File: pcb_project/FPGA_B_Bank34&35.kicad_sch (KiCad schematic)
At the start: 16 parts, among them U1 XC7A100T-FTG256

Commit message: LED & FPGA_Started
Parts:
- removed C26: 330µF, symbol Device:C
- removed C27, C28, C29, C30, C31, C32: 4.7µF, symbol Device:C
- removed C33, C34, C35, C36, C37, C38, C39, C40: 0.47µF, symbol Device:C
- removed U1: XC7A100T-FTG256, symbol FPGA_Xilinx_Artix7:XC7A100T-FTG256
- added U1: XC7A100T-FTG256, symbol FPGA_Xilinx_Artix7:XC7A100T-FTG256
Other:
- removed sheet A_Bank14&15
- removed sheet B_Bank34&35

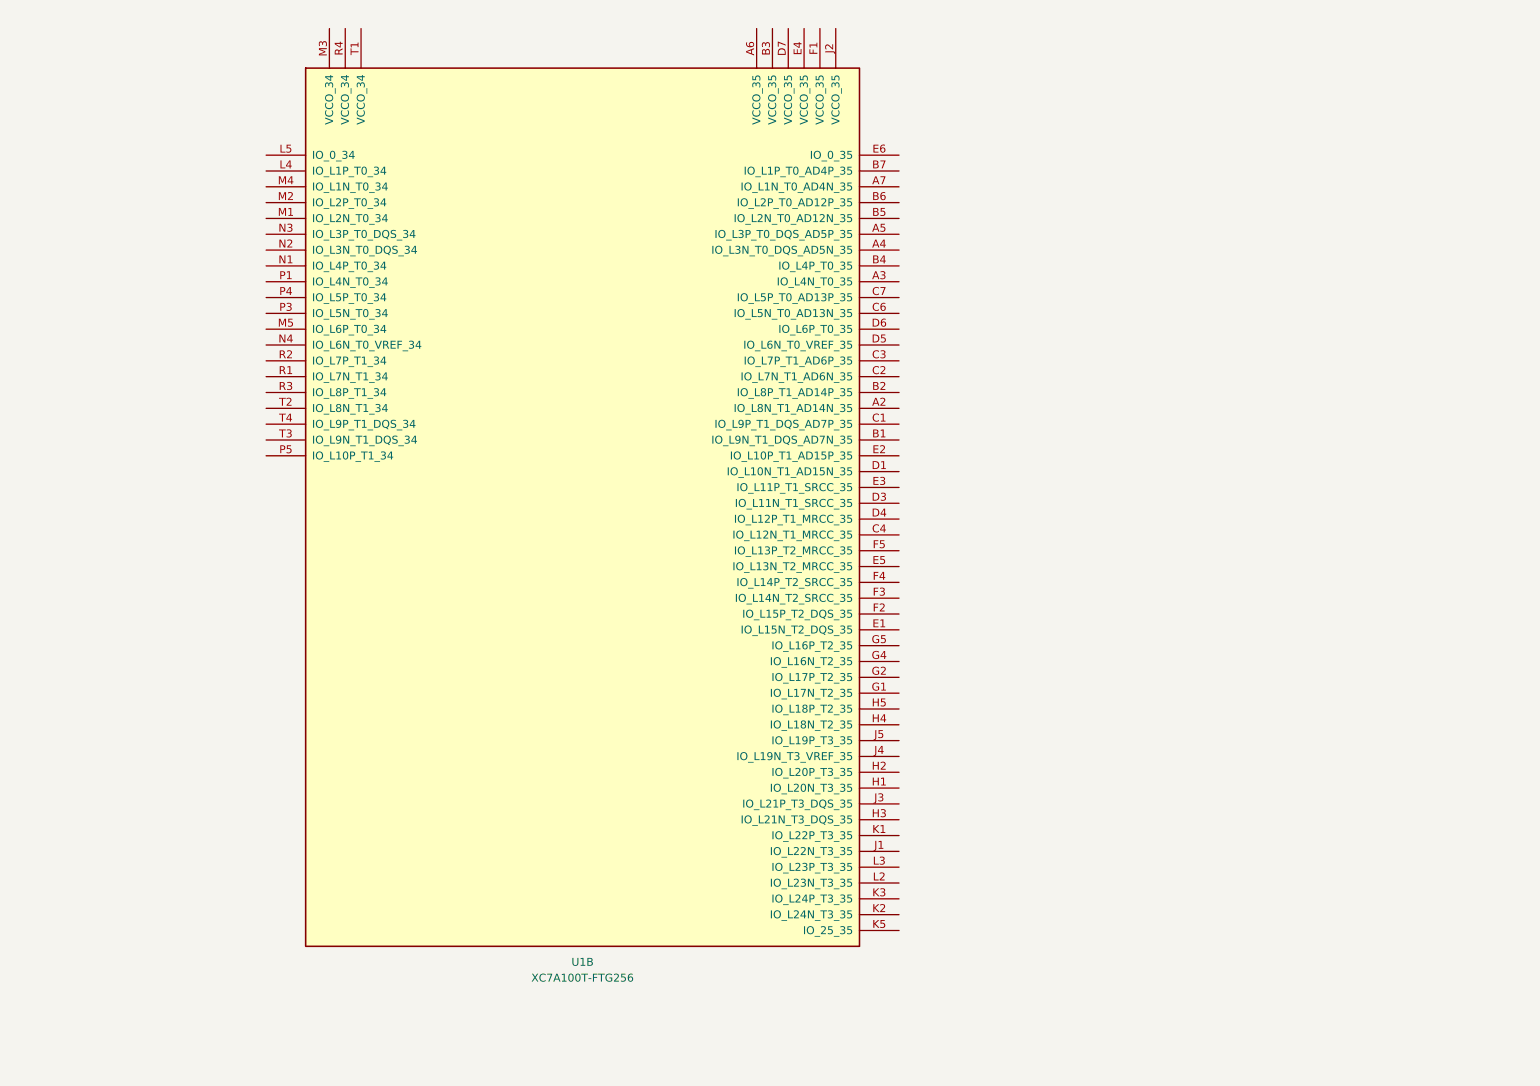
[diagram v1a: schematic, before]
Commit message: Crystal + SPI flash FPGA
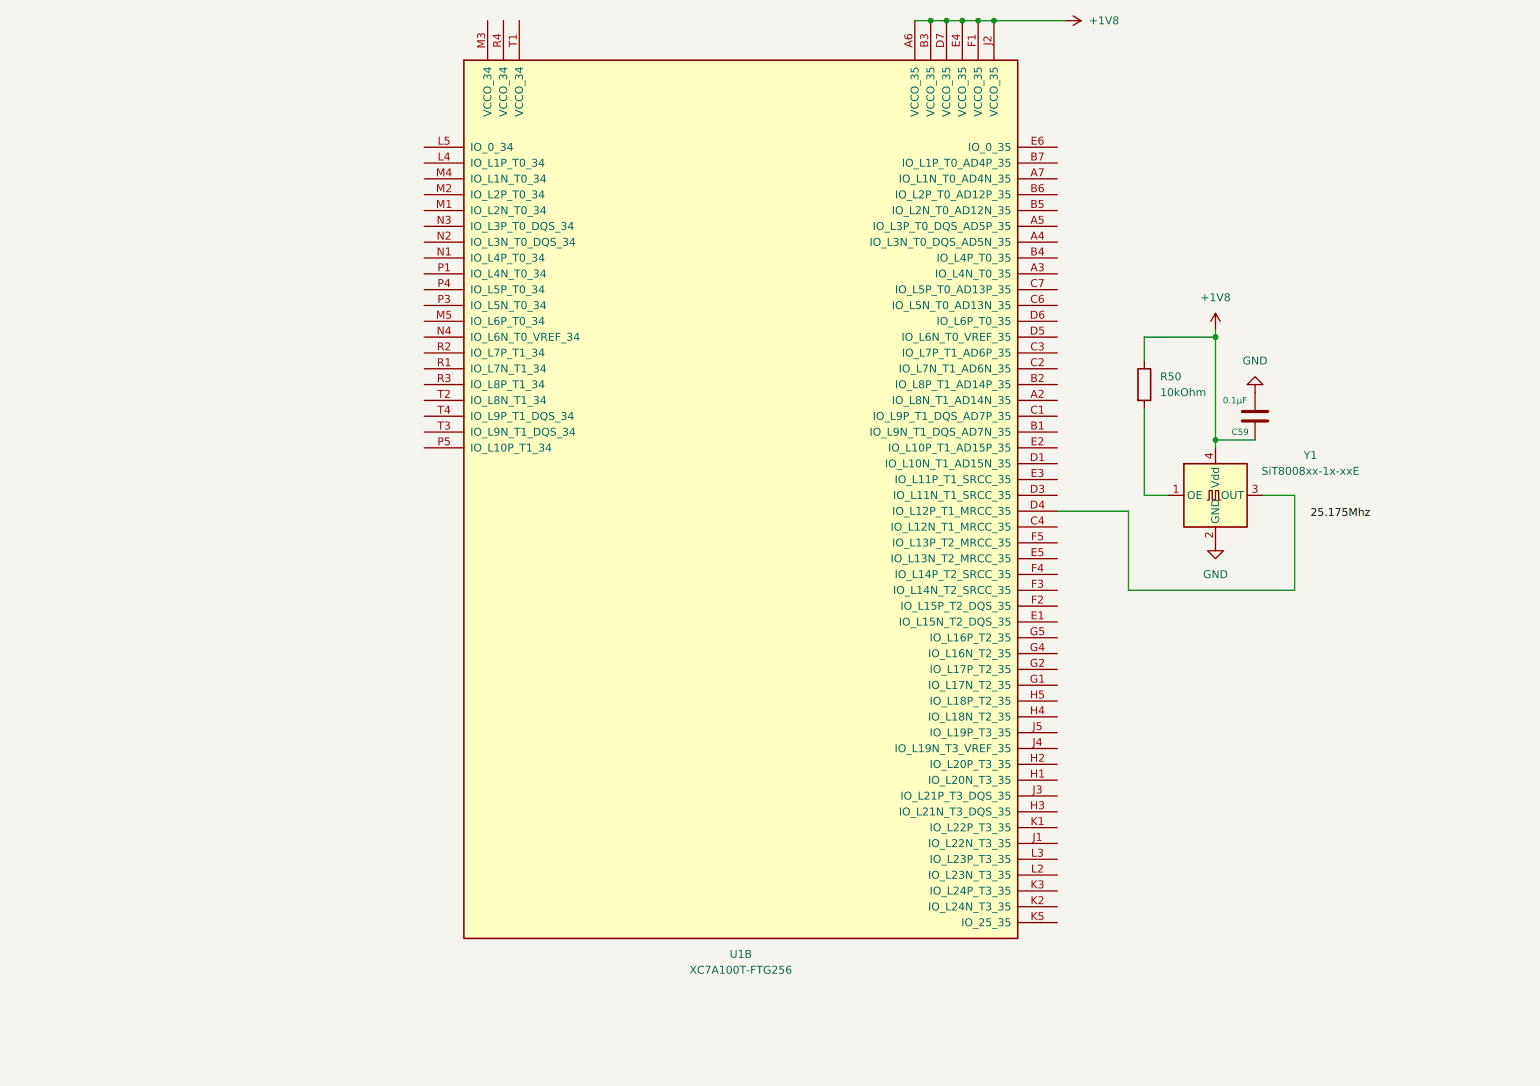
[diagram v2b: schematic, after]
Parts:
- added C59: 0.1µF, symbol Device:C
- added R50: 10kOhm, symbol Device:R
- added Y1: SiT8008xx-1x-xxE, Oscillator:Oscillator_SMD_SiT_PQFN-4Pin_2.5x2.0mm, symbol Oscillator:SiT8008xx-1x-xxE
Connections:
- net +1V8: now reaches U1.A6 (VCCO_35)
- net +1V8: now also U1.B3 (VCCO_35), U1.D7 (VCCO_35), U1.E4 (VCCO_35), U1.F1 (VCCO_35), U1.J2 (VCCO_35), C59.1, R50.1, Y1.4 (Vdd)
- net at U1.D4 (IO_L12P_T1_MRCC_35): now also Y1.3 (OUT)
- new net: R50.2, Y1.1 (OE)
- new net GND: C59.2, Y1.2 (GND)
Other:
- moved on the sheet: U1B

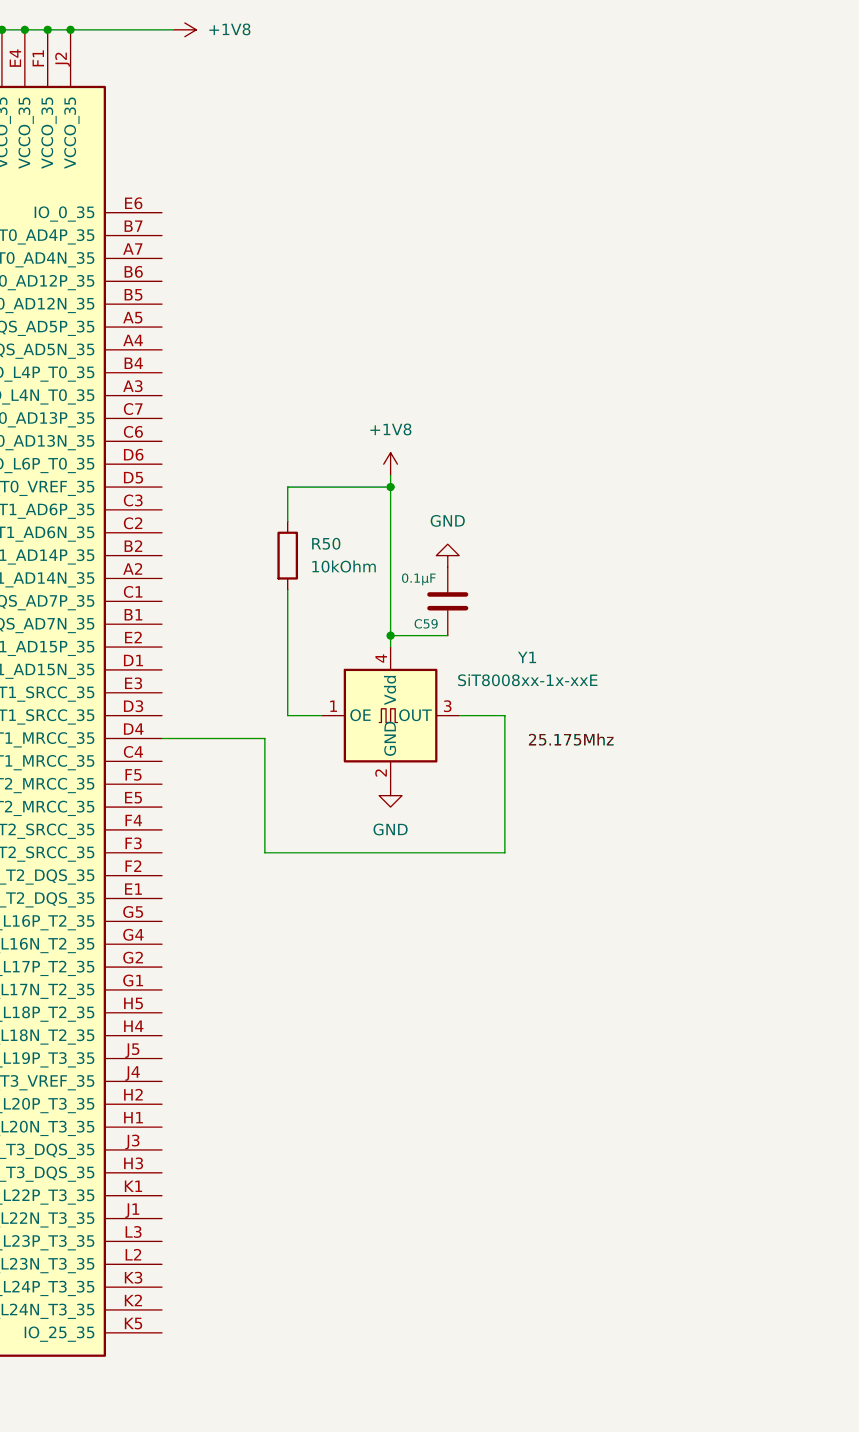
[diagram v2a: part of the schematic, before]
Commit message: VGA Root + Change FPGA Oscilator to 3.3v
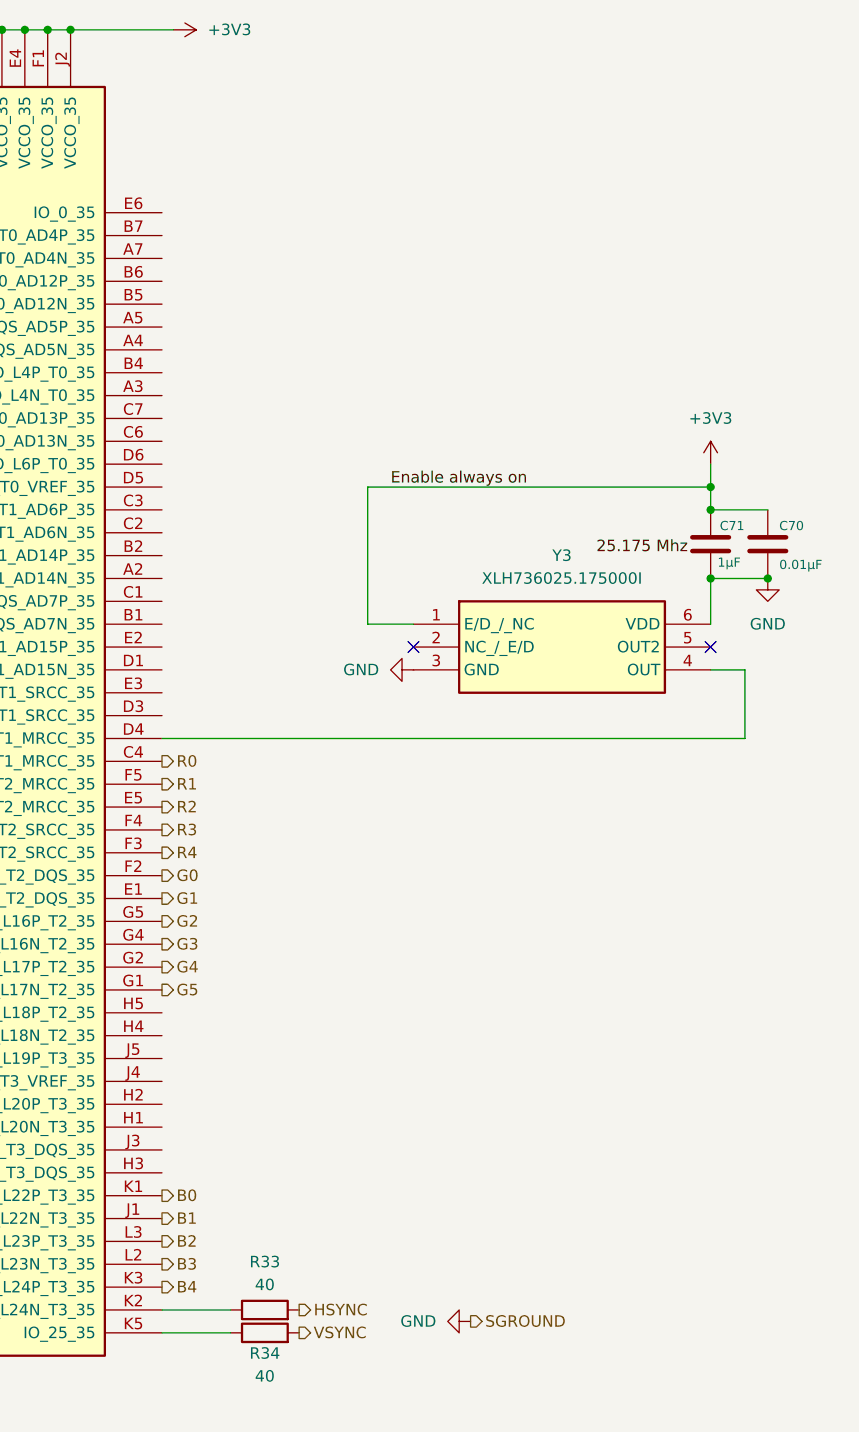
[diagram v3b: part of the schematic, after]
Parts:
- removed C59: 0.1µF, symbol Device:C
- removed R50: 10kOhm, symbol Device:R
- removed Y1: SiT8008xx-1x-xxE, Oscillator:Oscillator_SMD_SiT_PQFN-4Pin_2.5x2.0mm, symbol Oscillator:SiT8008xx-1x-xxE
- added C70: 0.01µF, symbol Device:C
- added C71: 1µF, symbol Device:C
- added R33, R34: 40, symbol Device:R
- added Y3: XLH736025.175000I, XLH730003580000I, symbol XLH736025_175000I:XLH736025.175000I
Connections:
- net GND: now also C70.2, C71.2, Y3.3 (GND), Y3.6 (VDD)
- net at U1.D4 (IO_L12P_T1_MRCC_35): now also Y3.4 (OUT)
- net R0: now reaches U1.C4 (IO_L12N_T1_MRCC_35)
- net G1: now reaches U1.E1 (IO_L15N_T2_DQS_35)
- net R2: now reaches U1.E5 (IO_L13N_T2_MRCC_35)
- net G0: now reaches U1.F2 (IO_L15P_T2_DQS_35)
- net R4: now reaches U1.F3 (IO_L14N_T2_SRCC_35)
- net R3: now reaches U1.F4 (IO_L14P_T2_SRCC_35)
- net R1: now reaches U1.F5 (IO_L13P_T2_MRCC_35)
- net G5: now reaches U1.G1 (IO_L17N_T2_35)
- net G4: now reaches U1.G2 (IO_L17P_T2_35)
- net G3: now reaches U1.G4 (IO_L16N_T2_35)
- net G2: now reaches U1.G5 (IO_L16P_T2_35)
- net B1: now reaches U1.J1 (IO_L22N_T3_35)
- net B0: now reaches U1.K1 (IO_L22P_T3_35)
- net at U1.K2 (IO_L24N_T3_35): now also R33.1
- net B4: now reaches U1.K3 (IO_L24P_T3_35)
- net at U1.K5 (IO_25_35): now also R34.1
- net B3: now reaches U1.L2 (IO_L23N_T3_35)
- net B2: now reaches U1.L3 (IO_L23P_T3_35)
- net +1V8 renamed +3V3
- net +3V3: now also C70.1, C71.1, Y3.1 (E/D_/_NC)
- new net HSYNC: R33.2
- new net VSYNC: R34.2
- no-connect marks 0 -> 2
